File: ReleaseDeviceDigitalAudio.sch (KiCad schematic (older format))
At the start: 8 parts, among them J3 AudioJack3, J4 AudioJack3, J5 AudioJack3, J7 AudioJack3, J8 AudioJack3

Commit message: Umsortiert
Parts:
- removed J?: Conn_02x08_Odd_Even, Connector_PinSocket_2.54mm:PinSocket_2x08_P2.54mm_Vertical, symbol Connector_Generic:Conn_02x08_Odd_Even
- removed J?: Conn_02x01, Connector_PinHeader_2.54mm:PinHeader_1x02_P2.54mm_Vertical, symbol Connector_Generic:Conn_02x01
- removed J?: Conn_01x03_Male, Connector_PinHeader_2.54mm:PinHeader_1x03_P2.54mm_Vertical, symbol Connector:Conn_01x03_Male
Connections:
- net labels removed: ButtonA2GND, DataEncoderDataAvailable, DataEncoderDataOutA, DataEncoderDataOutB, DataEncoderDataOutC, DataEncoderDataOutD, DataEncoderDataOutE, DataEncoderOutputEnable, KeyLock.A, KeyLock.B, LedGreenCathode, LedRedCathode, LedYellowCathode, OnSwitchLedAnode, Signal_Strength_Dial_+, UiLdr
- wire segments 88 -> 64
- no-connect marks 5 -> 4
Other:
- note removed: "Spiegelung um Längsachse nätig, je nach Orientierung"
- note removed: "UIBoard interfacing\n"

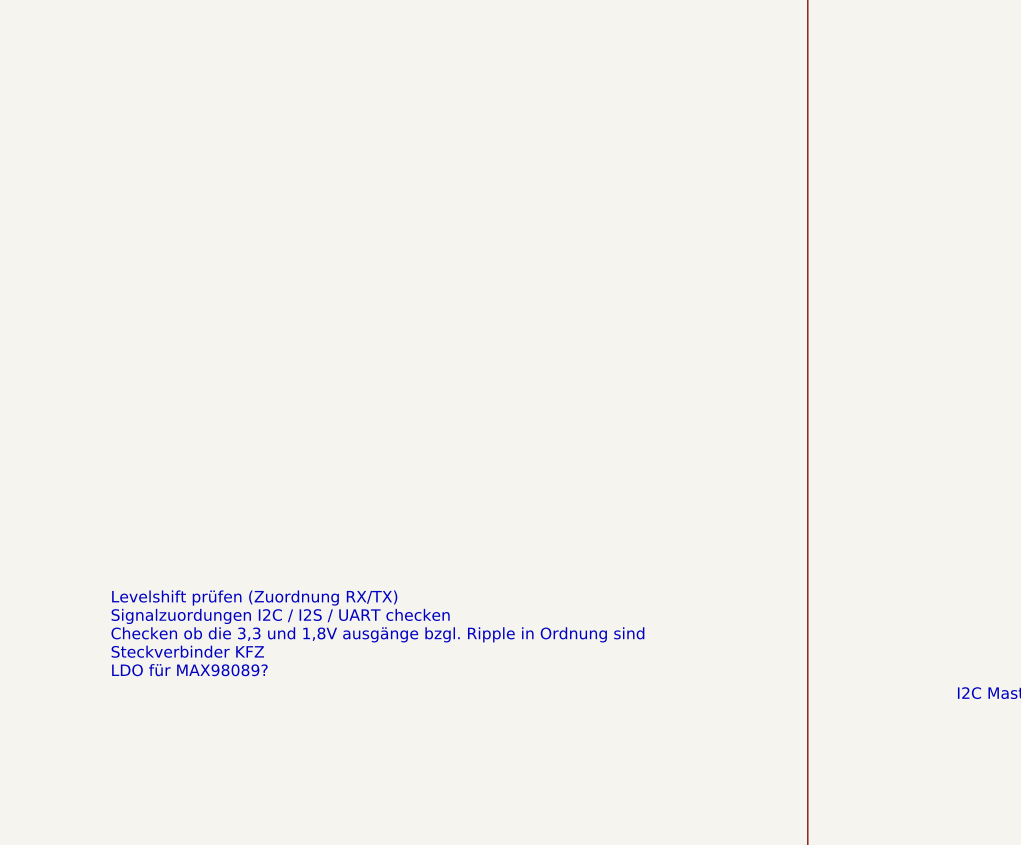
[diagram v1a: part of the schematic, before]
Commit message: - CM4 update - Todo Liste auf Hauptschaltplan hinzugefügt
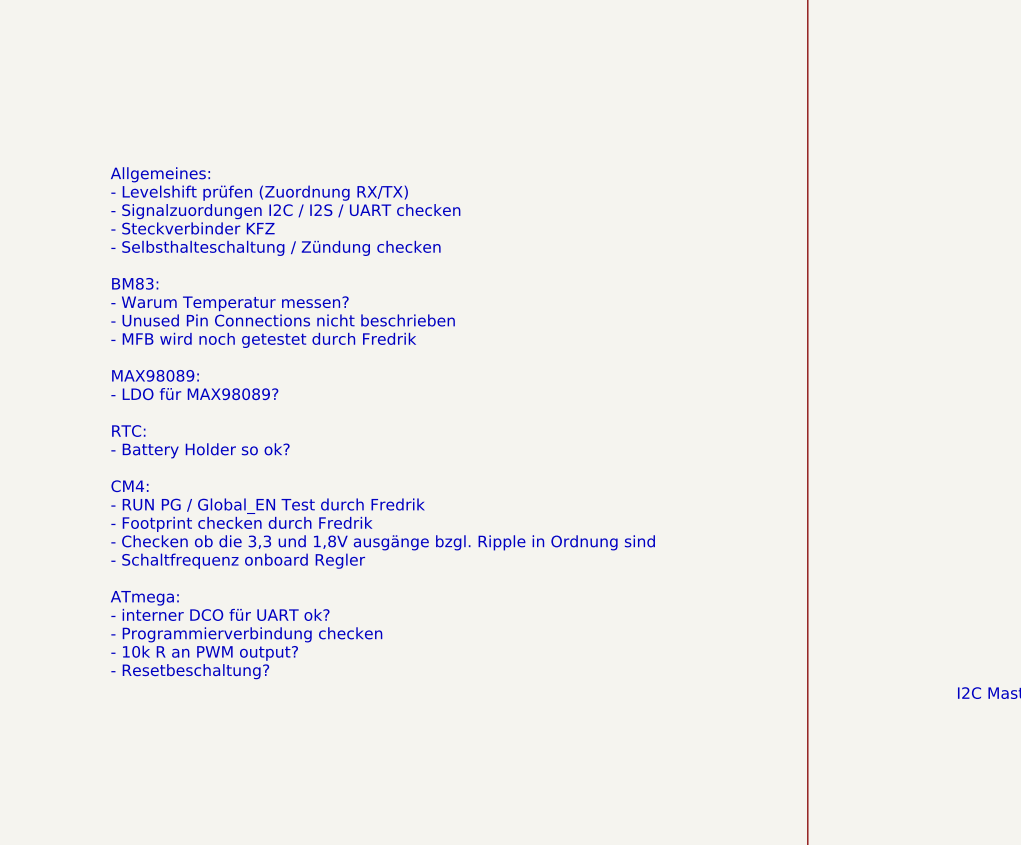
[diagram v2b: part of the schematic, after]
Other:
- note added: "Allgemeines: \n- Levelshift prüfen (Zuordnung RX/TX)\n- Signalzuordungen I2C / I2S / UART checken\n- Steckverbinder KFZ\n- Selbsthalteschaltung / Zündung checken\n\nBM83:\n- Warum Temperatur messen?\n- Unused Pin Connections nicht beschrieben\n- MFB wird noch getestet durch Fredrik\n\nMAX98089:\n- LDO für MAX98089?\n\nRTC:\n- Battery Holder so ok?\n\nCM4: \n- RUN PG / Global_EN Test durch Fredrik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"
- note removed: "Levelshift prüfen (Zuordnung RX/TX)\nSignalzuordungen I2C / I2S / UART checken\nChecken ob die 3,3 und 1,8V ausgänge bzgl. Ripple in Ordnung sind\nSteckverbinder KFZ\nLDO für MAX98089?\n"
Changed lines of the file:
@@
 	8800 2650 12000 2650
 Text Notes 900  6050 0    50   ~ 0
-Levelshift prüfen (Zuordnung RX/TX)\nSignalzuordungen I2C / I2S / UART checken\nChecken ob die 3,3 und 1,8V ausgänge bzgl. Ripple in Ordnung sind\nSteckverbinder KFZ\nLDO für MAX98089?\n
+Allgemeines: \n- Levelshift prüfen (Zuordnung RX/TX)\n- Signalzuordungen I2C / I2S / UART checken\n- Steckverbinder KFZ\n- Selbsthalteschaltung / Zündung checken\n\nBM83:\n- Warum Temperatur messen?\n- Unused Pin Connections nicht beschrieben\n- MFB wird noch getestet durch Fredrik\n\nMAX98089:\n- LDO für MAX98089?\n\nRTC:\n- Battery Holder so ok?\n\nCM4: \n- RUN PG / Global_EN Test durch Fredrik\n- Footprint checken durch Fredrik\n- Checken ob die 3,3 und 1,8V ausgänge bzgl. Ripple in Ordnung sind\n- Schaltfrequenz onboard Regler\n\nATmega:\n- interner DCO für UART ok?\n- Programmierverbindung checken\n- 10k R an PWM output?\n- Resetbeschaltung?\n
 $Comp
 L power:GND #PWR02

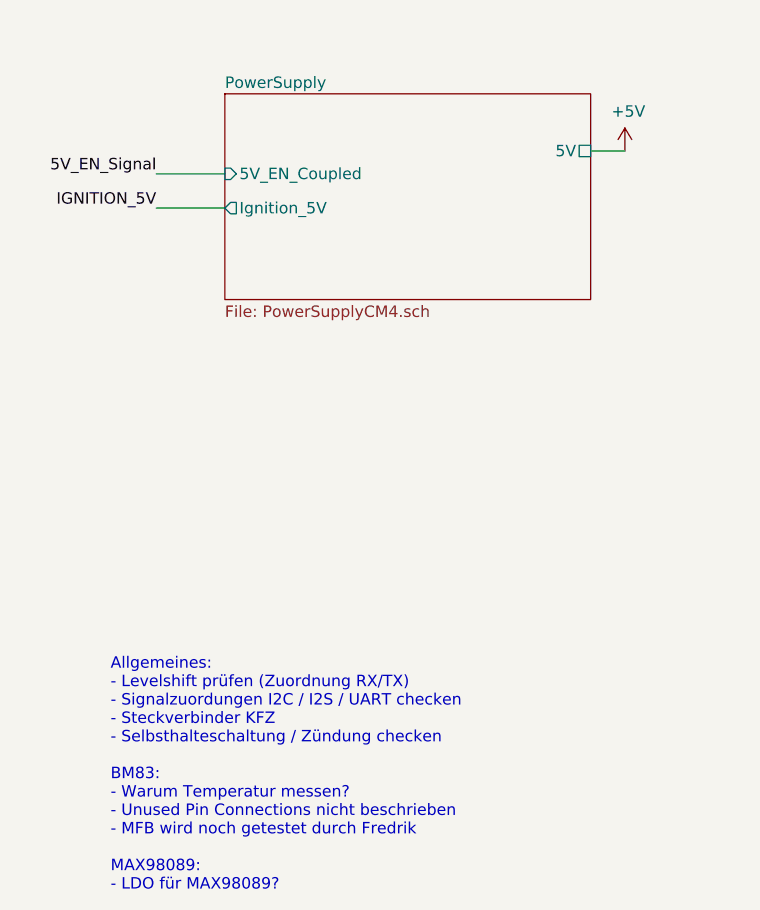
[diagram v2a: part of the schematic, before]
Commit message: - Selbsthalteschaltung vorerst fertig, Simulation folgt
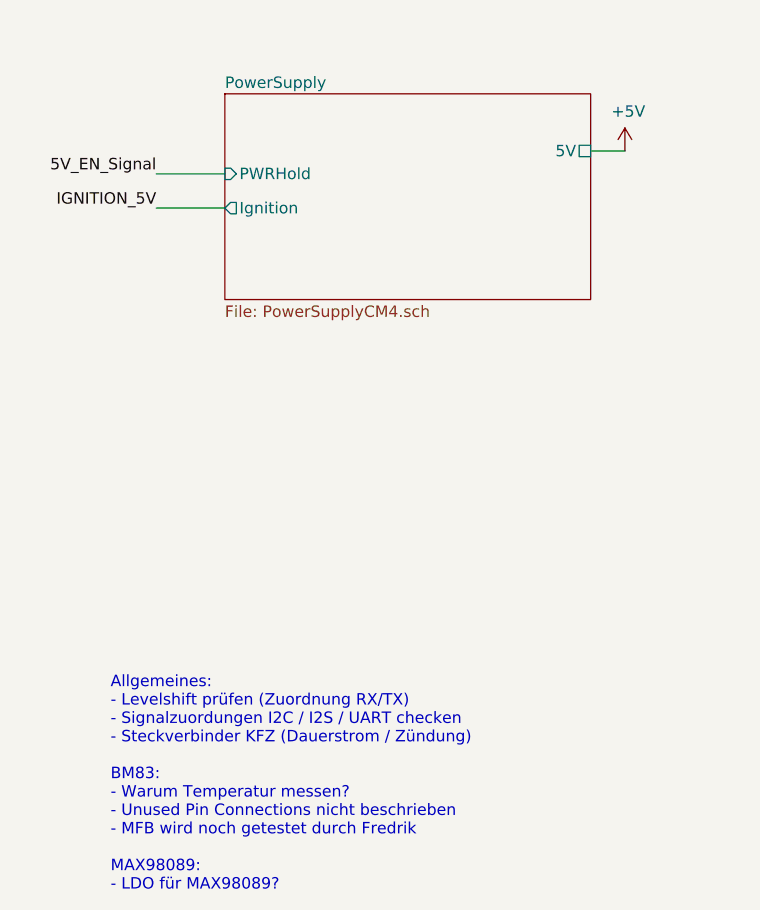
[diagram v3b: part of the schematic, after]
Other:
- note added: "Allgemeines: \n- Levelshift prüfen (Zuordnung RX/TX)\n- Signalzuordungen I2C / I2S / UART checken\n- Steckverbinder KFZ (Dauerstrom / Zündung)\n\nBM83:\n- Warum Temperatur messen?\n- Unused Pin Connections nicht beschrieben\n- MFB wird noch getestet durch Fredrik\n\nMAX98089:\n- LDO für MAX98089?\n\nRTC:\n- Battery Holder so ok?\n\nCM4: \n- RUN PG / Global_EN Test durch Fredrik\n- Footprint check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"
- note removed: "Allgemeines: \n- Levelshift prüfen (Zuordnung RX/TX)\n- Signalzuordungen I2C / I2S / UART checken\n- Steckverbinder KFZ\n- Selbsthalteschaltung / Zündung checken\n\nBM83:\n- Warum Temperatur messen?\n- Unused Pin Connections nicht beschrieben\n- MFB wird noch getestet durch Fredrik\n\nMAX98089:\n- LDO für MAX98089?\n\nRTC:\n- Battery Holder so ok?\n\nCM4: \n- RUN PG / Global_EN Test durch Fredrik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"
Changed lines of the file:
@@
 	8800 2650 12000 2650
 Text Notes 900  6050 0    50   ~ 0
-Allgemeines: \n- Levelshift prüfen (Zuordnung RX/TX)\n- Signalzuordungen I2C / I2S / UART checken\n- Steckverbinder KFZ\n- Selbsthalteschaltung / Zündung checken\n\nBM83:\n- Warum Temperatur messen?\n- Unused Pin Connections nicht beschrieben\n- MFB wird noch getestet durch Fredrik\n\nMAX98089:\n- LDO für MAX98089?\n\nRTC:\n- Battery Holder so ok?\n\nCM4: \n- RUN PG / Global_EN Test durch Fredrik\n- Footprint checken durch Fredrik\n- Checken ob die 3,3 und 1,8V ausgänge bzgl. Ripple in Ordnung sind\n- Schaltfrequenz onboard Regler\n\nATmega:\n- interner DCO für UART ok?\n- Programmierverbindung checken\n- 10k R an PWM output?\n- Resetbeschaltung?\n
+Allgemeines: \n- Levelshift prüfen (Zuordnung RX/TX)\n- Signalzuordungen I2C / I2S / UART checken\n- Steckverbinder KFZ (Dauerstrom / Zündung)\n\nBM83:\n- Warum Temperatur messen?\n- Unused Pin Connections nicht beschrieben\n- MFB wird noch getestet durch Fredrik\n\nMAX98089:\n- LDO für MAX98089?\n\nRTC:\n- Battery Holder so ok?\n\nCM4: \n- RUN PG / Global_EN Test durch Fredrik\n- Footprint checken durch Fredrik\n- Checken ob die 3,3 und 1,8V ausgänge bzgl. Ripple in Ordnung sind\n- Schaltfrequenz onboard Regler\n\nATmega:\n- interner DCO für UART ok?\n- Programmierverbindung checken\n- 10k R an PWM output?\n- Resetbeschaltung?\n
 $Comp
 L power:GND #PWR02
@@
 F2 "I2C_SDA" B L 7200 6050 50
 F3 "I2C_SCL" I L 7200 6150 50
-$EndSheet
-$Sheet
-S 1400 1350 1600 900
-U 64BEC8E8
-F0 "PowerSupply" 50
-F1 "PowerSupplyCM4.sch" 50
-F2 "5V" U R 3000 1600 50
-F3 "5V_EN_Coupled" I L 1400 1700 50
-F4 "Ignition_5V" O L 1400 1850 50
 $EndSheet
 Text Notes 7250 1500 0    50   ~ 0
@@
 F16 "I2S_SD_WS" B R 5550 2700 50
 $EndSheet
+$Sheet
+S 1400 1350 1600 900
+U 64BEC8E8
+F0 "PowerSupply" 50
+F1 "PowerSupplyCM4.sch" 50
+F2 "5V" U R 3000 1600 50
+F3 "PWRHold" I L 1400 1700 50
+F4 "Ignition" O L 1400 1850 50
+$EndSheet
 $EndSCHEMATC

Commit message: - ESD Schutz Zündung
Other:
- note added: "Allgemeines: \n- Levelshift prüfen (Zuordnung RX/TX)\n- Signalzuordungen I2C / I2S / UART checken\n- Steckverbinder KFZ (Dauerstrom / Zündung)\n\nSelbsthaltung:\n- Verhalten GPIO output bei undervoltage lockout\n\nBM83:\n- Warum Temperatur messen?\n- Unused Pin Connections nicht beschrieben\n- MFB wird noch getestet durch Fredrik\n\nMAX98089:\n- LDO für MAX98089?\n\nRTC:\n- Battery Holder so ok?\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"
- note removed: "Allgemeines: \n- Levelshift prüfen (Zuordnung RX/TX)\n- Signalzuordungen I2C / I2S / UART checken\n- Steckverbinder KFZ (Dauerstrom / Zündung)\n\nBM83:\n- Warum Temperatur messen?\n- Unused Pin Connections nicht beschrieben\n- MFB wird noch getestet durch Fredrik\n\nMAX98089:\n- LDO für MAX98089?\n\nRTC:\n- Battery Holder so ok?\n\nCM4: \n- RUN PG / Global_EN Test durch Fredrik\n- Footprint check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"
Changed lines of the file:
@@
 	8800 2650 12000 2650
 Text Notes 900  6050 0    50   ~ 0
-Allgemeines: \n- Levelshift prüfen (Zuordnung RX/TX)\n- Signalzuordungen I2C / I2S / UART checken\n- Steckverbinder KFZ (Dauerstrom / Zündung)\n\nBM83:\n- Warum Temperatur messen?\n- Unused Pin Connections nicht beschrieben\n- MFB wird noch getestet durch Fredrik\n\nMAX98089:\n- LDO für MAX98089?\n\nRTC:\n- Battery Holder so ok?\n\nCM4: \n- RUN PG / Global_EN Test durch Fredrik\n- Footprint checken durch Fredrik\n- Checken ob die 3,3 und 1,8V ausgänge bzgl. Ripple in Ordnung sind\n- Schaltfrequenz onboard Regler\n\nATmega:\n- interner DCO für UART ok?\n- Programmierverbindung checken\n- 10k R an PWM output?\n- Resetbeschaltung?\n
+Allgemeines: \n- Levelshift prüfen (Zuordnung RX/TX)\n- Signalzuordungen I2C / I2S / UART checken\n- Steckverbinder KFZ (Dauerstrom / Zündung)\n\nSelbsthaltung:\n- Verhalten GPIO output bei undervoltage lockout\n\nBM83:\n- Warum Temperatur messen?\n- Unused Pin Connections nicht beschrieben\n- MFB wird noch getestet durch Fredrik\n\nMAX98089:\n- LDO für MAX98089?\n\nRTC:\n- Battery Holder so ok?\n\nCM4: \n- RUN PG / Global_EN Test durch Fredrik\n- Footprint checken durch Fredrik\n- Checken ob die 3,3 und 1,8V ausgänge bzgl. Ripple in Ordnung sind\n- Schaltfrequenz onboard Regler\n\nATmega:\n- interner DCO für UART ok?\n- Programmierverbindung checken\n- 10k R an PWM output?\n- Resetbeschaltung?\n
 $Comp
 L power:GND #PWR02
